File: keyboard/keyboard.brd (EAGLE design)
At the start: 113 x 131.5 mm, 33 parts, among them SW1 CHERRY_MX, SW10 CHERRY_MX, SW11 CHERRY_MX, SW12 CHERRY_MX, SW13 CHERRY_MX, SW14 CHERRY_MX, SW15 CHERRY_MX, SW16 CHERRY_MX, SW17 CHERRY_MX, SW18 CHERRY_MX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

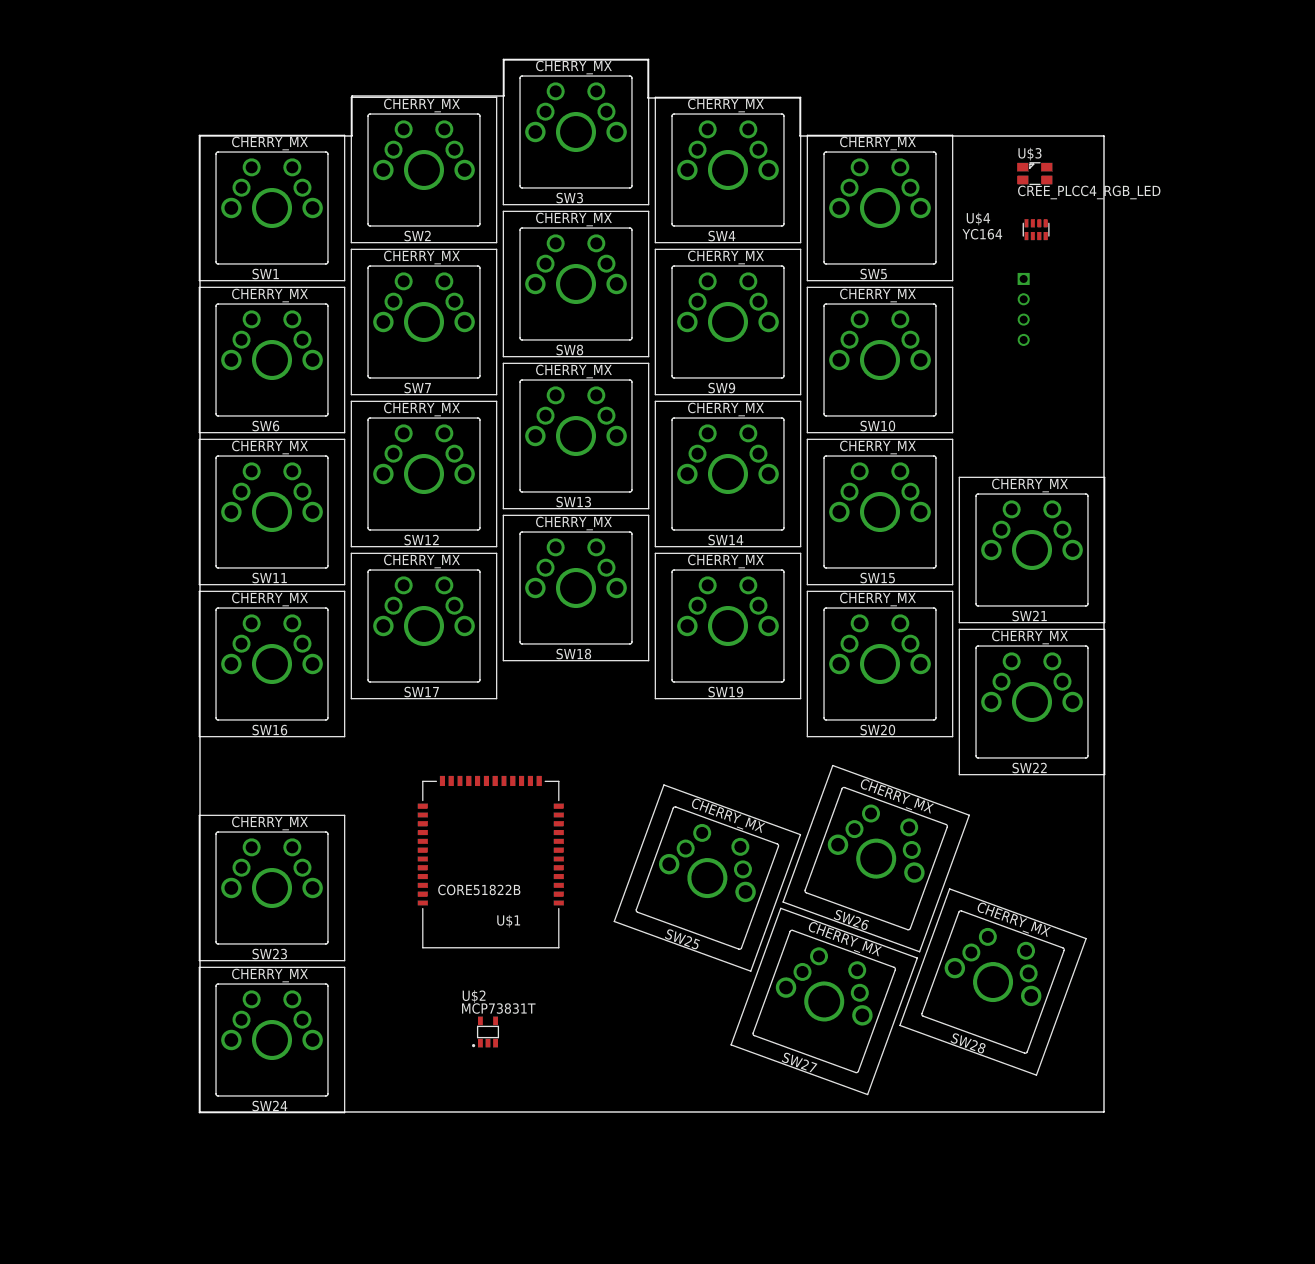
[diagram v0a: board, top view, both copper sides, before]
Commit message: connect mcp73831t charging circuit
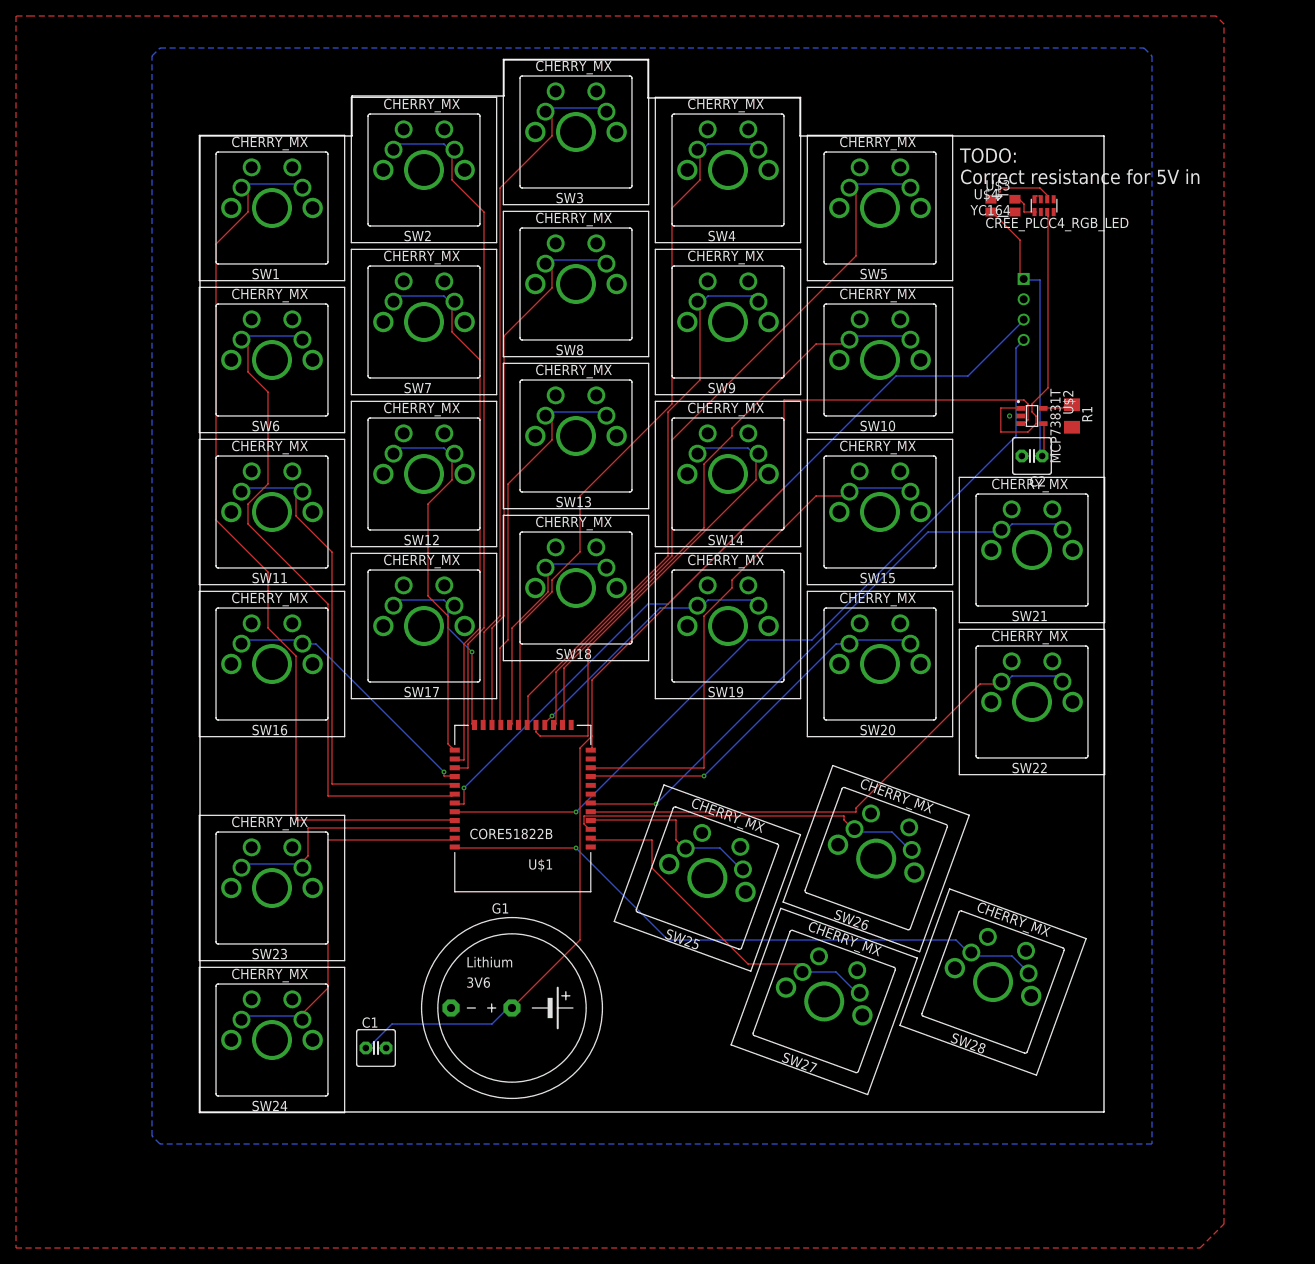
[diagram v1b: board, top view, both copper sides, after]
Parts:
- added C1, C2: 4.7uF, capacitor-wima:C2.5-5
- added G1: SL-340/P3.6V, battery:SL-340/P3.6V
- added R1: 2k, resistor:M1206
- moved U$2 102.7 mm to (104.0, 87.0), turned to 270 degrees
- moved U$1 8.06 mm to (40.4, 37.9)
- moved U$3 5.66 mm to (100.4, 113.3)
- moved U$4 3.16 mm to (105.5, 113.3)
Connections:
- new net GREEN: U$3.GREEN, U$4.P$5
- new net N$3: U$4.P$1, U$4.P$2
- new net PROG: R1.1, U$2.5-PROG
- new net RED: U$3.RED, U$4.P$3
- new net RSINK: U$2.1-STAT, U$4.P$7
- new net VIN: C2.1, U$2.4VDD, U$3.ANODE, U$5.VCC
- net GND: now also C1.2, C2.2, G1.-, R1.2, U$2.2-VSS, U$4.P$6
- net VCC: now also C1.1, G1.+, U$2.3-VBAT; no longer U$5.VCC
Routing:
- net VCC: track 0.00 -> 146.1 mm
- net SW1: track 0.00 -> 113.3 mm
- net SWCLK: track 0.00 -> 102.1 mm, vias 0 -> 1
- net SWDIO: track 0.00 -> 97.5 mm, vias 0 -> 1
- net SW5: track 0.00 -> 91.5 mm
- net SW2: track 0.00 -> 89.7 mm
- net SW4: track 0.00 -> 89.6 mm
- net SW3: track 0.00 -> 88.8 mm
- net SW6: track 0.00 -> 87.8 mm
- net SW28: track 0.00 -> 78.5 mm, vias 0 -> 1
- net SW21: track 0.00 -> 73.8 mm, vias 0 -> 1
- net SW10: track 0.00 -> 73.6 mm
- net SW9: track 0.00 -> 70.1 mm
- net SW8: track 0.00 -> 69.4 mm
- net SW7: track 0.00 -> 69.1 mm
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- added copper zone on layer 1, net GND
- added copper zone on layer 16, net GND
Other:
- board text added: "TODO: Correct resistance for 5V in"

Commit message: update resistors
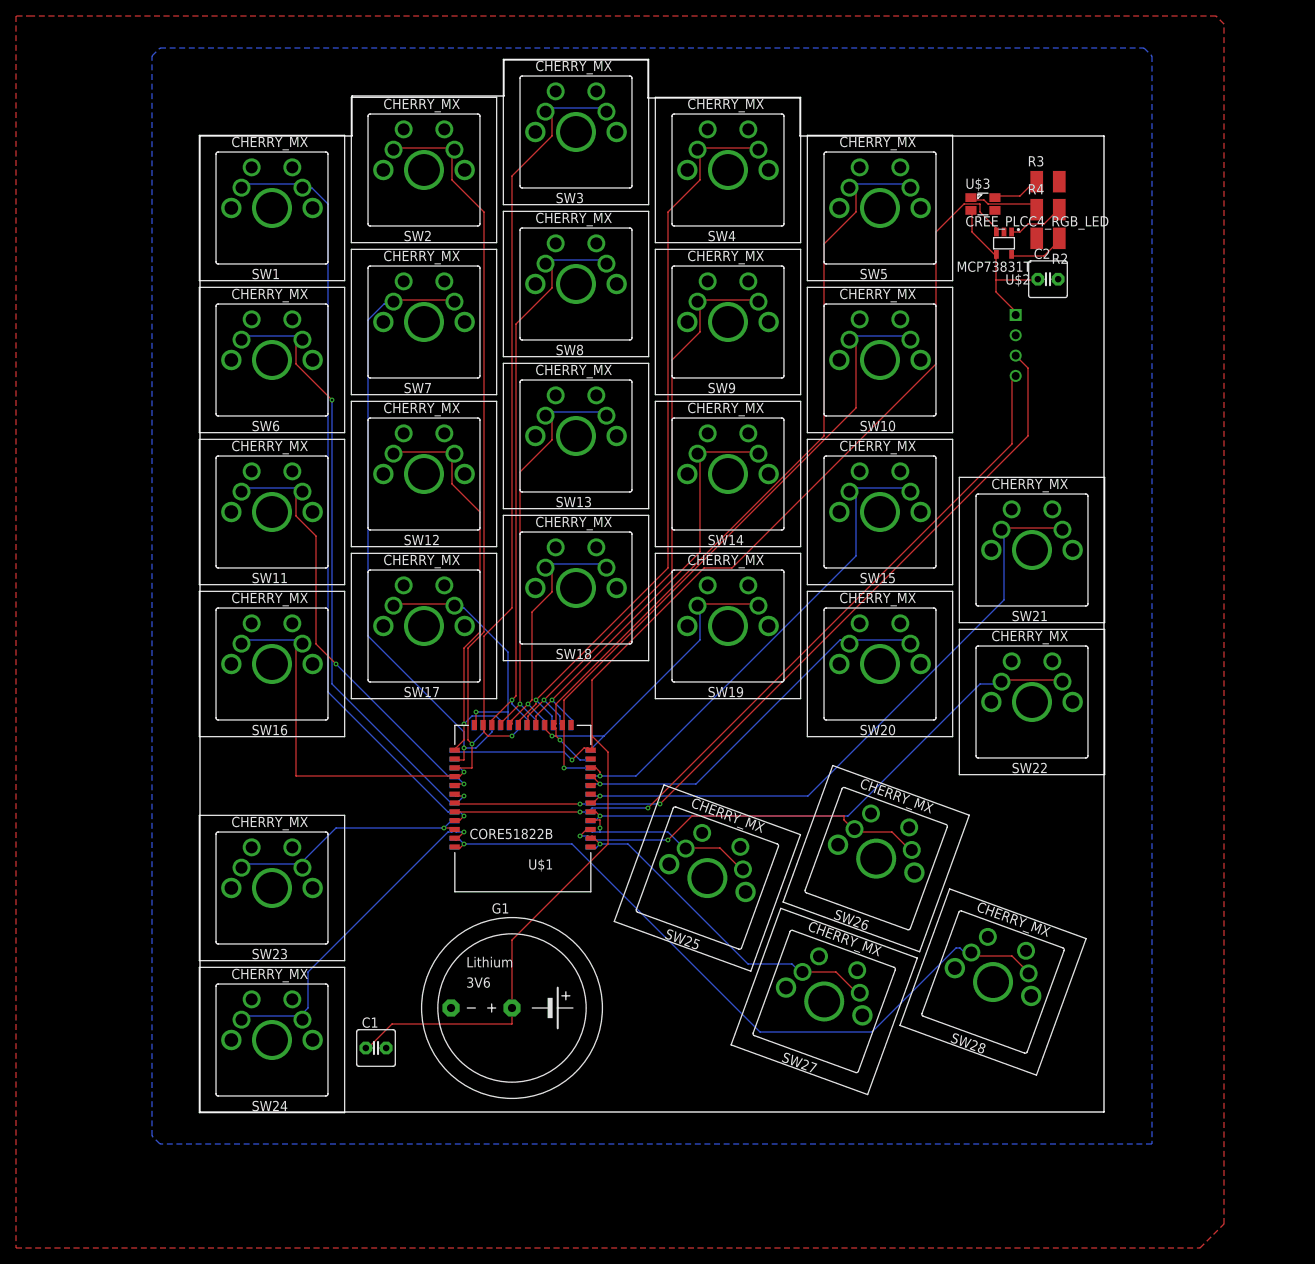
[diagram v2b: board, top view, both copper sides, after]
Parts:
- removed R1: 2k, resistor:M1206
- removed U$4: YC164, yc164:YC164
- added R2, R3, R4: (no value), resistor:R1210
- added U$6: CORE51822B, core51822b:CORE51822B
- moved C2 22.2 mm to (106.0, 104.1), turned to 0 degrees
- moved U$2 21.9 mm to (100.5, 108.6), turned to 180 degrees
- moved U$5 4.61 mm to (102.0, 99.6)
- moved U$3 2.51 mm to (97.9, 113.5)
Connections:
- removed net N$3: U$4.P$1, U$4.P$2
- net GND: now also R2.2, R3.2, U$6.GND0, U$6.GND1; no longer R1.2, U$4.P$6
- net GREEN: now also R3.1; no longer U$4.P$5
- net PROG: now also R2.1; no longer R1.1
- net RED: now also R4.1; no longer U$4.P$3
- net RSINK: now also R4.2; no longer U$4.P$7
- net SW1: now also U$6.P24
- net SW10: now also U$6.P13
- net SW11: now also U$6.P28
- net SW12: now also U$6.P02
- net SW13: now also U$6.P06
- net SW14: now also U$6.P10
- net SW15: now also U$6.P14
- net SW16: now also U$6.P29
- net SW17: now also U$6.P03
- net SW18: now also U$6.P07
- net SW19: now also U$6.P11
- net SW2: now also U$6.P00
- net SW20: now also U$6.P15
- net SW21: now also U$6.P16
- net SW22: now also U$6.P17
- net SW23: now also U$6.P23
- net SW24: now also U$6.P22
- net SW25: now also U$6.P18
- net SW26: now also U$6.P19
- net SW27: now also U$6.P20
- net SW28: now also U$6.P21
- net SW3: now also U$6.P04
- net SW4: now also U$6.P08
- net SW5: now also U$6.P12
- net SW6: now also U$6.P25
- net SW7: now also U$6.P01
- net SW8: now also U$6.P05
- net SW9: now also U$6.P09
- net SWCLK: now also U$6.SWCLK
- net SWDIO: now also U$6.SWDIO
- net VCC: now also U$6.VCC
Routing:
- net RSINK: track 37.9 -> 7.09 mm
- net VCC: track 146.1 -> 175.6 mm, vias 0 -> 1
- net VIN: track 38.9 -> 20.8 mm
- net SW1: track 113.3 -> 97.9 mm, vias 0 -> 1
- net SW16: track 34.3 -> 47.8 mm
- net SW28: track 78.5 -> 89.5 mm
- net SW6: track 87.8 -> 77.9 mm, vias 0 -> 2
- net SW7: track 69.1 -> 78.3 mm, vias 0 -> 1
- net SW10: track 73.6 -> 80.7 mm, vias 0 -> 1
- net SW5: track 91.5 -> 98.5 mm, vias 0 -> 1
- net SW11: track 62.4 -> 55.7 mm, vias 0 -> 2
- net SW17: track 25.2 -> 31.8 mm
- net SW3: track 88.8 -> 95.3 mm, vias 0 -> 1
- net SW21: track 73.8 -> 80.2 mm
- net SW19: track 33.7 -> 39.9 mm
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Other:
- board text removed: "TODO: Correct resistance for 5V in"

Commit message: add GRM32ER71H475KA88L capacitor
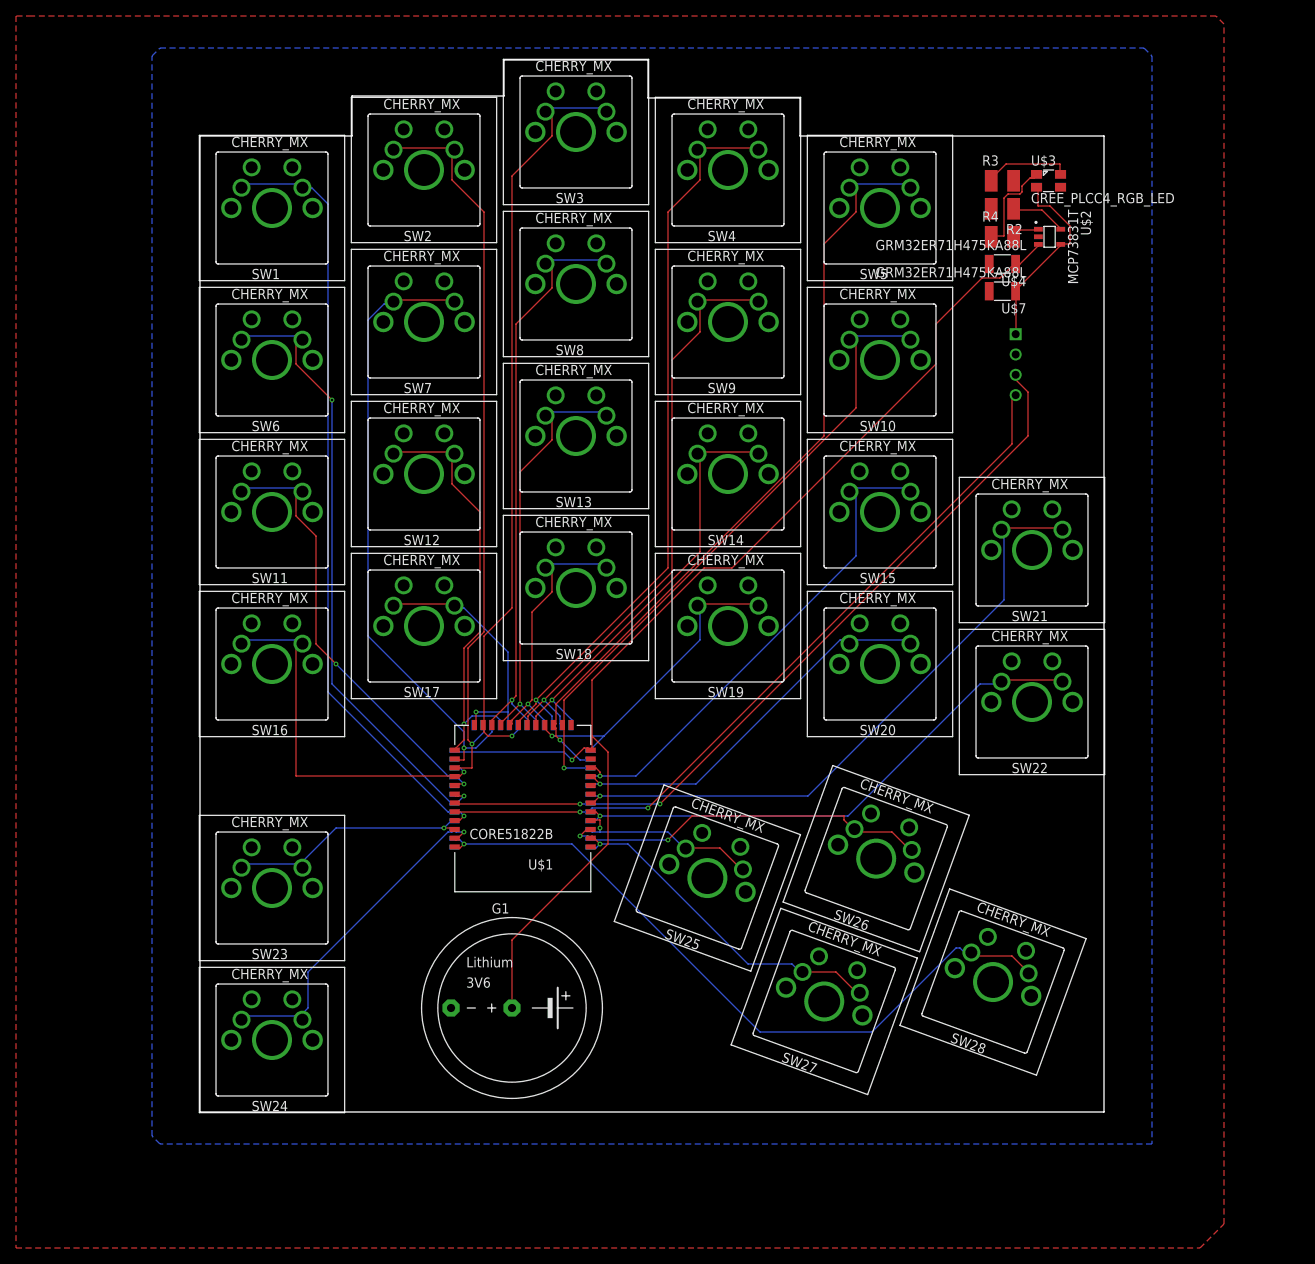
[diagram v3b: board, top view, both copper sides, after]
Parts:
- removed C1, C2: 4.7uF, capacitor-wima:C2.5-5
- added U$4, U$7: GRM32ER71H475KA88L, GRM32ER71H475KA88L:GRM32ER71H475KA88L
- R2, R3, R4: value (none) -> 2k
- moved U$3 8.70 mm to (106.1, 116.4)
- moved R2 6.80 mm to (100.3, 112.9)
- moved R4 6.64 mm to (100.3, 109.4)
- moved U$2 5.76 mm to (106.2, 109.4), turned to 270 degrees
- moved R3 5.70 mm to (100.3, 116.4)
- moved U$5 2.40 mm to (102.0, 97.2)
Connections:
- net GND: now also U$4.P$2, U$7.P$2; no longer C1.2, C2.2
- net VCC: now also U$4.P$1; no longer C1.1
- net VIN: now also U$7.P$1; no longer C2.1
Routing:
- net VCC: track 175.6 -> 148.2 mm
- net GREEN: track 6.29 -> 11.1 mm
- net VIN: track 20.8 -> 24.4 mm
- net RSINK: track 7.09 -> 3.53 mm
- net RED: track 8.96 -> 12.2 mm
- net SWCLK: track 98.0 -> 95.5 mm
- net SWDIO: track 101.5 -> 99.1 mm
